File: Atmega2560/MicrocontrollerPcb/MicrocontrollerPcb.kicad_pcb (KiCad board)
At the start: 2 copper layers, 68.6 x 48.3 mm, 27 parts, among them J1 Conn_02x12_Odd_Even, U1 ATmega2560-16AU

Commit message: self
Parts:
- removed USBasp1: Conn_02x03_Odd_Even, Connector_PinHeader_2.54mm:PinHeader_2x03_P2.54mm_Vertical
- added 16MHz2: Crystal, Crystal:Crystal_HC49-U_Vertical, F.Cu at (157.5, 84.0)
- added C10: 22pF, Capacitor_SMD:C_0805_2012Metric_Pad1.15x1.40mm_HandSolder, F.Cu at (168.1, 81.1)
- added C11: 100n, Capacitor_SMD:C_0603_1608Metric_Pad1.05x0.95mm_HandSolder, F.Cu at (156.7, 70.1)
- added C12: 100n, Capacitor_SMD:C_0603_1608Metric_Pad1.05x0.95mm_HandSolder, F.Cu at (145.7, 102.9)
- added C8: 100n, Capacitor_SMD:C_0603_1608Metric_Pad1.05x0.95mm_HandSolder, F.Cu at (145.0, 86.5)
- added C9: 22pF, Capacitor_SMD:C_0805_2012Metric_Pad1.15x1.40mm_HandSolder, F.Cu at (153.0, 84.4)
- added D2: LED, LED_SMD:LED_1206_3216Metric, F.Cu at (163.0, 69.6)
- added D3: LED, LED_SMD:LED_1206_3216Metric, F.Cu at (166.4, 69.4)
- added FB1: Ferrite_Bead, Resistor_SMD:R_0805_2012Metric, F.Cu at (151.8, 68.3)
- added J2: USB_B_Micro, Connector_USB:USB_Micro-B_Amphenol_10103594-0001LF_Horizontal, F.Cu at (148.2, 74.8)
- added L1: L, Inductor_SMD:L_1812_4532Metric_Pad1.30x3.40mm_HandSolder, F.Cu at (147.8, 81.9)
- added R10: 1K, Resistor_SMD:R_1206_3216Metric_Pad1.42x1.75mm_HandSolder, F.Cu at (169.1, 75.8)
- added R11: 1K, Resistor_SMD:R_1206_3216Metric_Pad1.42x1.75mm_HandSolder, F.Cu at (168.1, 73.0)
- added R12: 1K, Resistor_SMD:R_1206_3216Metric_Pad1.42x1.75mm_HandSolder, F.Cu at (160.0, 69.5)
- added R13: 1K, Resistor_SMD:R_1206_3216Metric_Pad1.42x1.75mm_HandSolder, F.Cu at (169.1, 69.4)
- added R7: 1M, Resistor_SMD:R_0402_1005Metric, F.Cu at (159.4, 80.5)
- added R8: 22R, Resistor_SMD:R_0603_1608Metric_Pad1.05x0.95mm_HandSolder, F.Cu at (152.3, 72.6)
- added R9: 22R, Resistor_SMD:R_0603_1608Metric_Pad1.05x0.95mm_HandSolder, F.Cu at (152.5, 76.1)
- added RV1: Varistor, Resistor_SMD:R_0603_1608Metric_Pad1.05x0.95mm_HandSolder, F.Cu at (154.1, 73.0)
- added RV2: Varistor, Resistor_SMD:R_0603_1608Metric_Pad1.05x0.95mm_HandSolder, F.Cu at (152.7, 79.2)
- added U2: ATmega8U2-MU, Package_DFN_QFN:QFN-32-1EP_5x5mm_P0.5mm_EP3.1x3.1mm, F.Cu at (159.3, 75.3)
- C1, R5: moved to B.Cu
- C3: value 100n -> 22pF; footprint Capacitor_SMD:C_0603_1608Metric_Pad1.05x0.95mm_HandSolder -> Capacitor_SMD:C_0805_2012Metric_Pad1.15x1.40mm_HandSolder
- C6: value 22pF -> 100n; footprint Capacitor_SMD:C_0805_2012Metric_Pad1.15x1.40mm_HandSolder -> Capacitor_SMD:C_0603_1608Metric_Pad1.05x0.95mm_HandSolder
- R1: value 10k -> 1M
- R2: value 1M -> 10k; moved to B.Cu
- R4: value 10K -> 1K; footprint Resistor_SMD:R_0402_1005Metric -> Resistor_SMD:R_1206_3216Metric_Pad1.42x1.75mm_HandSolder
- R6: value 1K -> 10K; footprint Resistor_SMD:R_1206_3216Metric_Pad1.42x1.75mm_HandSolder -> Resistor_SMD:R_0402_1005Metric; moved to B.Cu
- moved R6 44.5 mm to (170.3, 103.6), turned to 180 degrees
- moved INPUT1 41.7 mm to (151.1, 109.2)
- moved C6 34.6 mm to (145.7, 97.5), turned to 0 degrees
- moved C4 34.2 mm to (196.1, 87.6), turned to 90 degrees
- moved R2 34.1 mm to (177.9, 104.4), turned to 0 degrees
- moved C7 32.3 mm to (145.7, 105.4)
- moved C5 32.1 mm to (145.7, 100.2)
- moved Servo3 27.2 mm to (202.7, 96.2)
- moved D1 26.0 mm to (147.3, 86.9), turned to 90 degrees
- moved LogicConverter1 24.5 mm to (170.7, 109.8)
- moved C1 20.7 mm to (177.7, 101.7), turned to 90 degrees
- moved R1 20.3 mm to (173.3, 87.8), turned to 90 degrees
- moved Servo4 20.1 mm to (202.5, 81.1)
- moved PressureSensor1 19.9 mm to (158.8, 87.6)
- moved J1 19.6 mm to (206.2, 107.0)
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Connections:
- C1 pad 1: Net-(16MHz1-Pad1) -> /Reset
- C2 pad 1: Net-(16MHz1-Pad2) -> Net-(16MHz1-Pad1)
- C3 pad 1: Net-(C3-Pad1) -> Net-(16MHz1-Pad2)
- C4 pad 1: Earth -> Net-(C4-Pad1)
- C4 pad 2: +5V -> Earth
- C6 pad 1: /Reset -> Earth
- C6 pad 2: Earth -> +5V
- J1 pad 24: Earth -> /Reset
- LogicConverter1 pad 1: /SCL -> /SDA
- LogicConverter1 pad 2: /SDA -> /SCL
- R1 pad 1: +5V -> Net-(16MHz1-Pad1)
- R1 pad 2: /Reset -> Net-(16MHz1-Pad2)
- R2 pad 1: Net-(16MHz1-Pad1) -> +5V
- R2 pad 2: Net-(16MHz1-Pad2) -> /Reset
- R4 pad 2: /SCL -> Net-(D1-Pad2)
- R5 pad 2: /SDA -> /SCL
- R6 pad 2: Net-(D1-Pad2) -> /SDA
- Servo1 pad 1: Net-(Servo1-Pad1) -> /S2
- Servo2 pad 1: /S2 -> /S4
- Servo3 pad 1: /S3 -> Net-(Servo3-Pad1)
- Servo4 pad 1: /S4 -> /S3
- Thrusters1 pad 10: /T7 -> Earth
- Thrusters1 pad 6: Earth -> /T6
- Thrusters1 pad 7: Earth -> /T7
- Thrusters1 pad 8: /T6 -> /T8
- Thrusters1 pad 9: /T8 -> Earth
- U1 pad 1: Net-(Servo1-Pad1) -> Net-(Servo3-Pad1)
- U1 pad 15: /T1 -> /T5
- U1 pad 16: /T2 -> /T4
- U1 pad 17: /T3 -> /T8
- U1 pad 18: /T4 -> /T7
- U1 pad 2: Net-(U1-Pad2) -> /RX0
- U1 pad 20: /SCK -> Net-(U1-Pad20)
- U1 pad 21: /MOSI -> Net-(U1-Pad21)
- U1 pad 22: /MISO -> Net-(U1-Pad22)
- U1 pad 23: /T5 -> /T6
- U1 pad 24: /T6 -> /T3
- U1 pad 25: /T7 -> /T2
- U1 pad 26: /T8 -> /T1
- U1 pad 3: Net-(U1-Pad3) -> /TX0
- U1 pad 98: Net-(C3-Pad1) -> Net-(C4-Pad1)
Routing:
- net +5V: track 42.1 -> 178.3 mm, vias 4 -> 5
- net Earth: track 86.9 -> 129.6 mm, vias 5 -> 0
- net Net-(J2-Pad1): track 0.00 -> 34.4 mm
- net /RX0: track 0.00 -> 33.9 mm, vias 0 -> 2
- net /TX0: track 0.00 -> 25.5 mm, vias 0 -> 2
- net /SCK: track 24.5 -> 0.00 mm
- net /T8: track 29.1 -> 6.13 mm, vias 2 -> 0
- net Net-(FB1-Pad2): track 0.00 -> 22.7 mm
- net /MOSI: track 21.8 -> 0.00 mm
- net /T6: track 26.9 -> 6.76 mm, vias 2 -> 0
- net /MISO: track 20.1 -> 0.00 mm
- net /USBVCC: track 0.00 -> 19.4 mm
- net Net-(C11-Pad2): track 0.00 -> 18.2 mm, vias 0 -> 2
- net /T7: track 22.9 -> 6.27 mm, vias 2 -> 0
- net Net-(Servo3-Pad1): track 0.00 -> 15.9 mm
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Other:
- board size 68.6 x 48.3 mm -> 65.4 x 46.4 mm

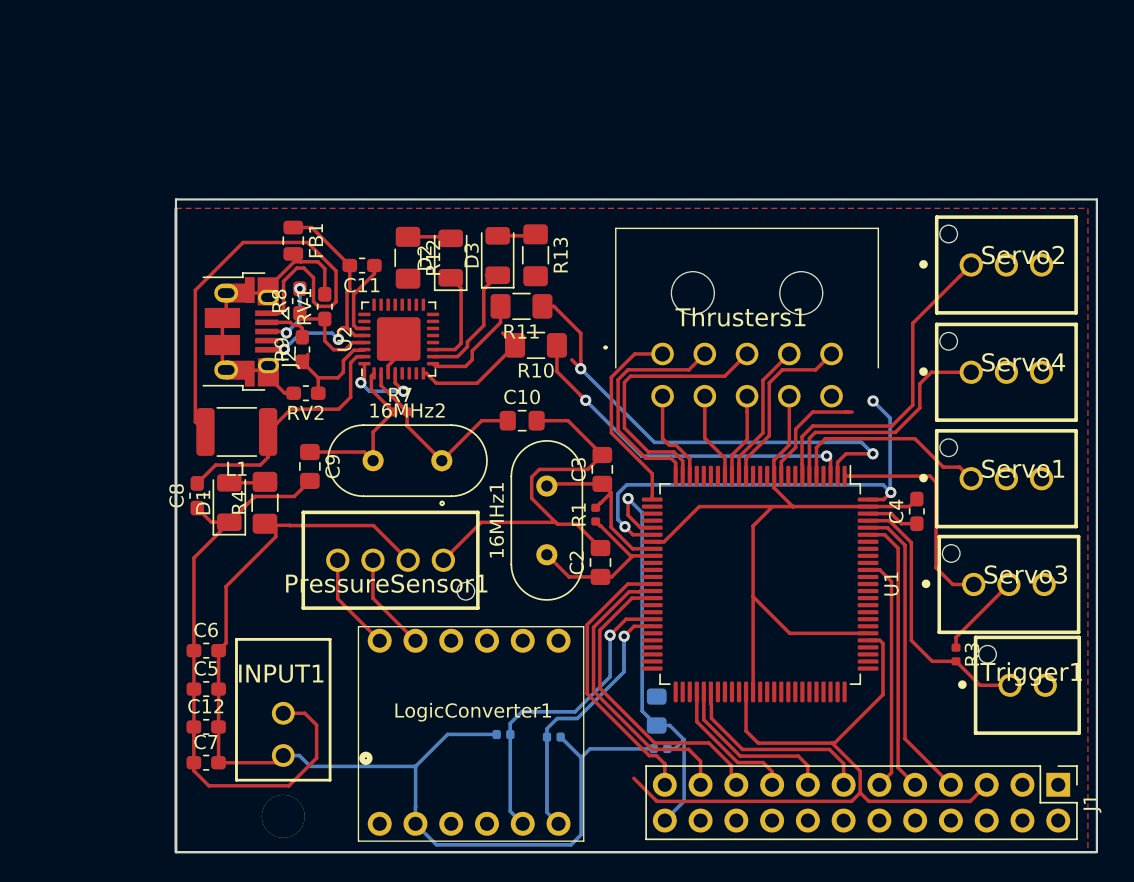
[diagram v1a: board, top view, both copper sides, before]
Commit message: Changed component Inductor->Fuse
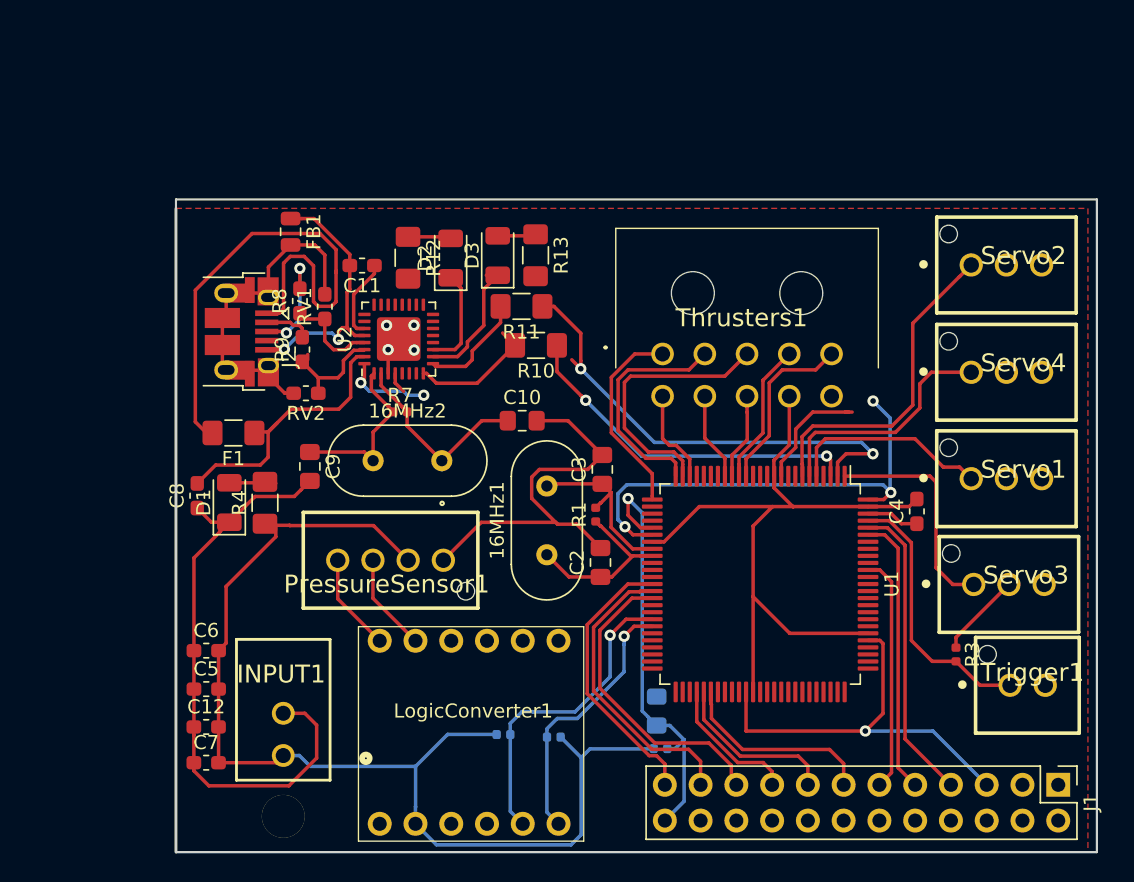
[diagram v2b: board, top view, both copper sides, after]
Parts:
- removed L1: L, Inductor_SMD:L_1812_4532Metric_Pad1.30x3.40mm_HandSolder
- added F1: 500mA, Fuse:Fuse_1206_3216Metric_Pad1.42x1.75mm_HandSolder, F.Cu at (147.6, 82.0)
- moved FB1 0.67 mm to (151.7, 67.7)
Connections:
- U2 pad 3: Net-(U2-Pad3) -> Earth
- U2 pad 33: Net-(U2-Pad3) -> Earth
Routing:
- net +5V: track 178.3 -> 159.0 mm, vias 5 -> 6
- net Net-(F1-Pad2): track 34.4 -> 37.9 mm
- net Net-(J2-Pad3): track 4.97 -> 7.86 mm
- net Earth: track 129.6 -> 132.4 mm, vias 0 -> 4
- net Net-(U2-Pad3): track 2.75 -> 0.00 mm
- net Net-(FB1-Pad2): track 22.7 -> 25.0 mm
- net Net-(C11-Pad2): track 18.2 -> 19.1 mm

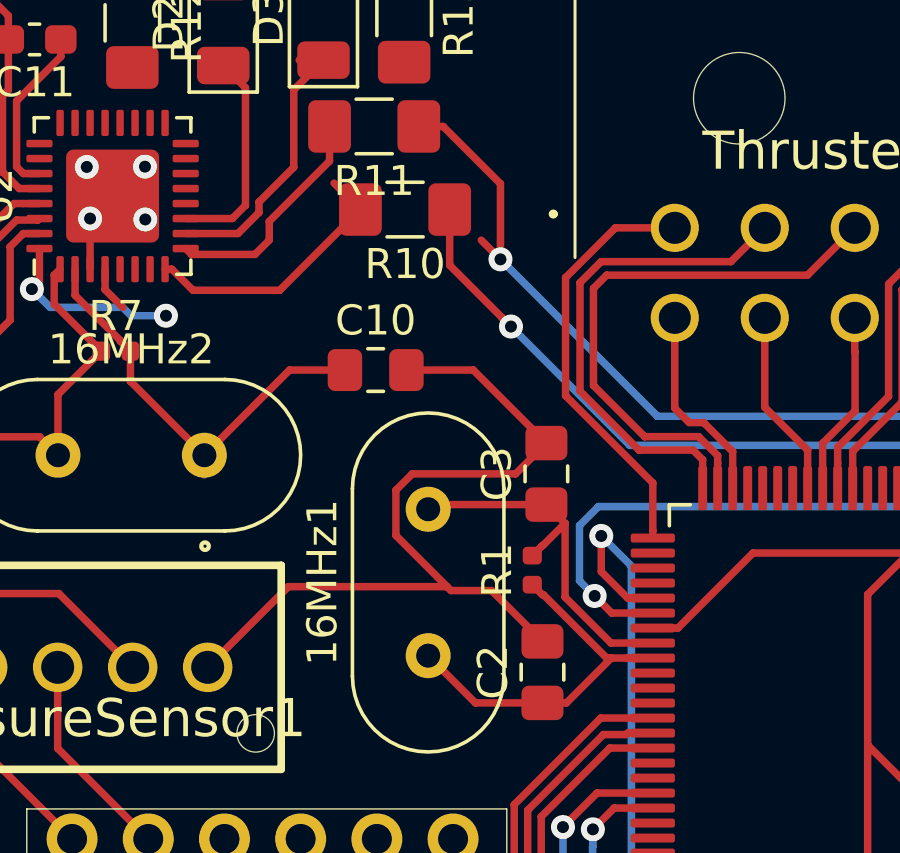
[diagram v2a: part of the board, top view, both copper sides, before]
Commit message: Removed Trace error
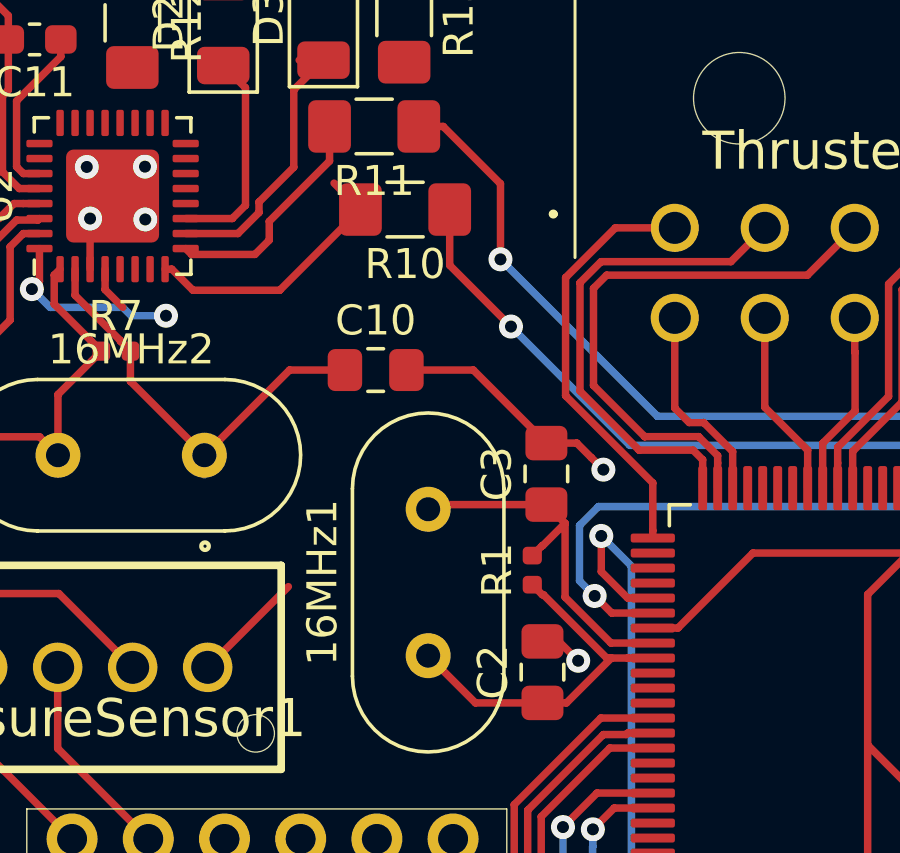
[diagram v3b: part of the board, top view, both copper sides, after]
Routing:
- net Earth: track 132.4 -> 117.3 mm, vias 4 -> 6
- net /RX0: track 33.9 -> 33.0 mm
